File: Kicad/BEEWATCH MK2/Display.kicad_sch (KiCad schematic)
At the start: 6 parts, among them J3 Conn_02x06_Odd_Even, Q2 DMG6968U

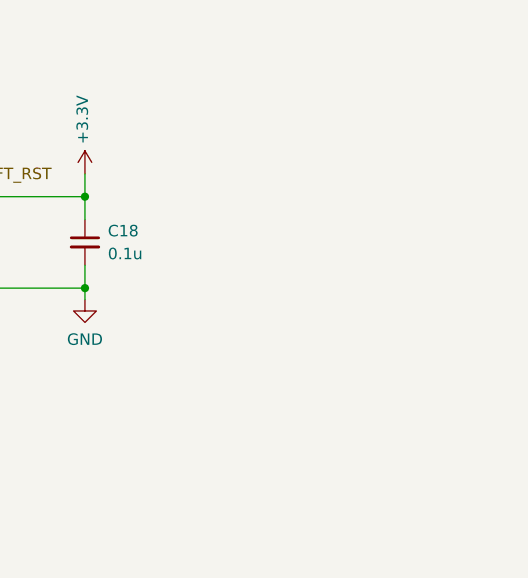
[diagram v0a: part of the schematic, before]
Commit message: Schematic changes
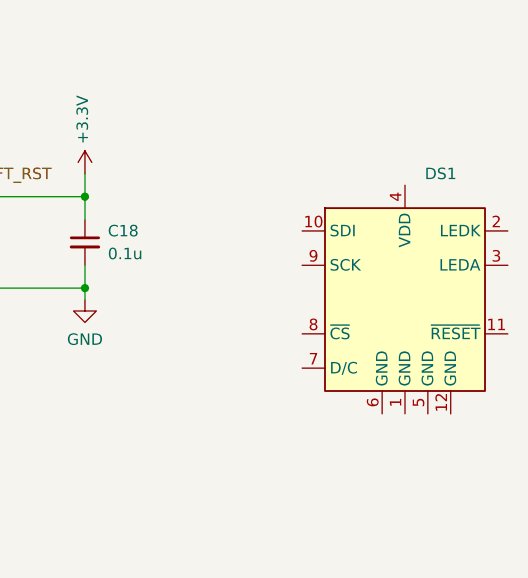
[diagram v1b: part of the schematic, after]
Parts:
- added DS1: ~, Project:GC9A01_TOP, symbol Project_Library:GC9A01
- R17, R18, R19: footprint Resistor_SMD:R_0402_1005Metric -> Resistor_SMD:R_0402_1005Metric_Pad0.72x0.64mm_HandSolder
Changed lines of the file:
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@@
 			)
 		)
-		(property "Footprint" "Resistor_SMD:R_0402_1005Metric"
+		(property "Footprint" "Resistor_SMD:R_0402_1005Metric_Pad0.72x0.64mm_HandSolder"
 			(at 100.33 109.22 0)
 			(effects
@@
 	)
 	(symbol
+		(lib_id "Project_Library:GC9A01")
+		(at 219.71 104.14 0)
+		(unit 1)
+		(exclude_from_sim no)
+		(in_bom yes)
+		(on_board yes)
+		(dnp no)
+		(fields_autoplaced yes)
+		(property "Reference" "DS1"
+			(at 221.9041 91.44 0)
+			(effects
+				(font
+					(size 1.27 1.27)
+				)
+				(justify left)
+			)
+		)
+		(property "Value" "~"
+			(at 221.9041 93.98 0)
+			(effects
+				(font
+					(size 1.27 1.27)
+				)
+				(justify left)
+			)
+		)
+		(property "Footprint" "Project:GC9A01_TOP"
+			(at 219.71 104.14 0)
+			(effects
+				(font
+					(size 1.27 1.27)
+				)
+				(hide yes)
+			)
+		)
+		(property "Datasheet" ""
+			(at 219.71 104.14 0)
+			(effects
+				(font
+					(size 1.27 1.27)
+				)
+				(hide yes)
+			)
+		)
+		(property "Description" ""
+			(at 219.71 104.14 0)
+			(effects
+				(font
+					(size 1.27 1.27)
+				)
+				(hide yes)
+			)
+		)
+		(pin "2"
+		)
+		(pin "8"
+		)
+		(pin "12"
+		)
+		(pin "1"
+		)
+		(pin "4"
+		)
+		(pin "5"
+		)
+		(pin "9"
+		)
+		(pin "3"
+		)
+		(pin "11"
+		)
+		(pin "10"
+		)
+		(pin "7"
+		)
+		(pin "6"
+		)
+		(instances
+			(project ""
+				(path "/e9c5fb53-480b-4989-8495-a3341ee99514/15b9618d-10d4-4333-8312-f49228536273"
+					(reference "DS1")
+					(unit 1)
+				)
+			)
+		)
+	)
+	(symbol
 		(lib_id "Device:R_Small")
 		(at 100.33 127 0)
@@
 			)
 		)
-		(property "Footprint" "Resistor_SMD:R_0402_1005Metric"
+		(property "Footprint" "Resistor_SMD:R_0402_1005Metric_Pad0.72x0.64mm_HandSolder"
 			(at 100.33 127 0)
 			(effects
@@
 			)
 		)
-		(property "Footprint" "Resistor_SMD:R_0402_1005Metric"
+		(property "Footprint" "Resistor_SMD:R_0402_1005Metric_Pad0.72x0.64mm_HandSolder"
 			(at 142.24 91.44 0)
 			(effects
